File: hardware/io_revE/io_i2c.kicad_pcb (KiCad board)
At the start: 2 copper layers, 103.6 x 74.9 mm, 61 parts, among them J1 extra CS, J12 Conn_01x01, J13 Conn_01x01, J14 Conn_01x01, J15 Conn_01x01, J16 Target Interface, 2716 Pinout, J2 Jumper Block, J3 Jumper Block, J4 Target Interface, 2716 Pinout, J5 read region, J6 Conn_01x01, J7 Conn_01x01, J8 Conn_01x01, Q1 2N7000, U1 2716, U2 74LS74, U3 74LS125, U4 74LS138, U6 MCP23018-E_SP, U7 74LS138

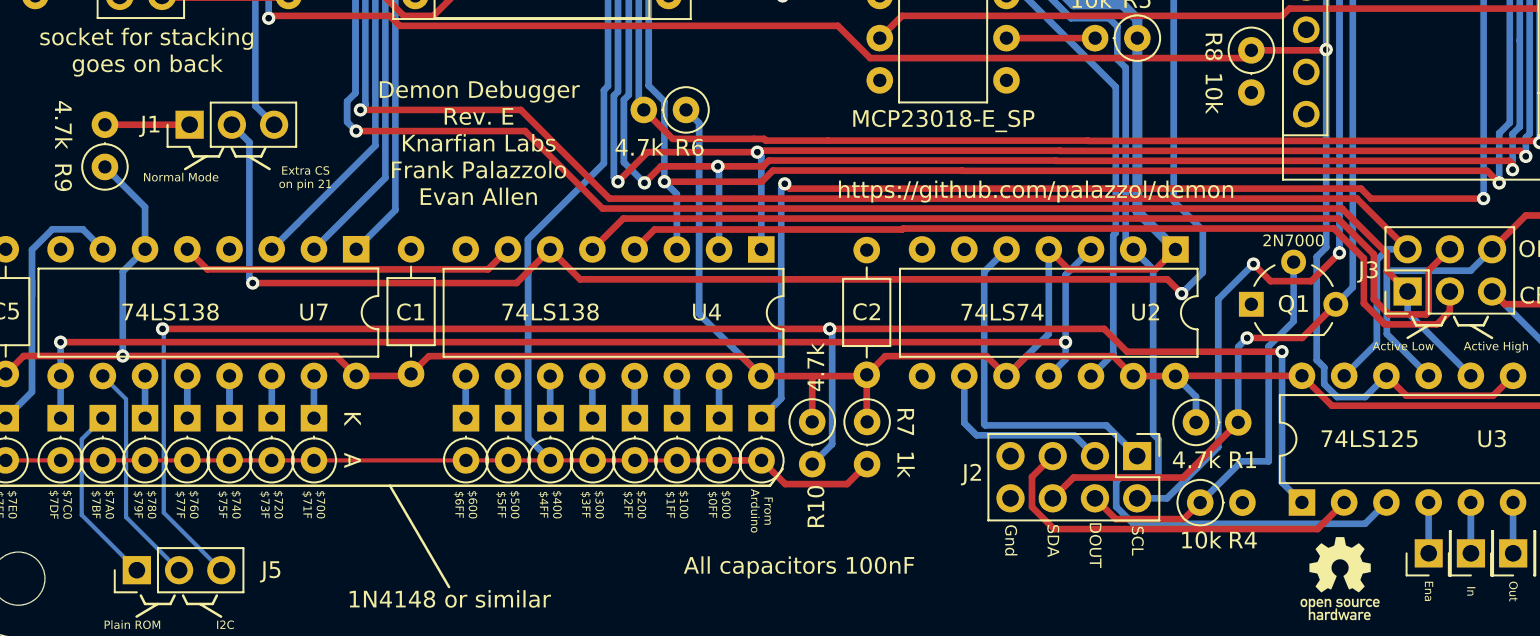
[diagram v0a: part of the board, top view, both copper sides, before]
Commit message: added pull up and silk changes
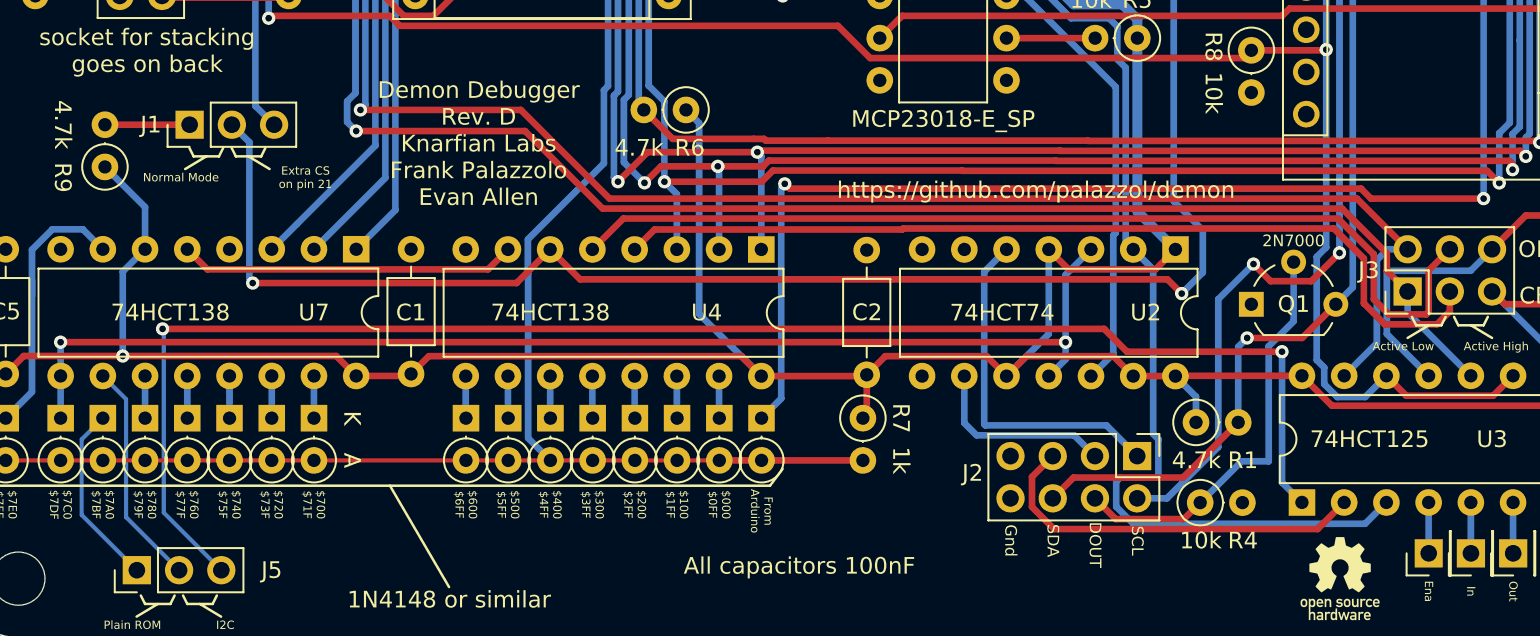
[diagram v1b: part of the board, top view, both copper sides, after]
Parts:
- removed R10: 4.7k, Resistor_THT:R_Axial_DIN0207_L6.3mm_D2.5mm_P2.54mm_Vertical
- U2: value 74LS74 -> 74HCT74
- U3: value 74LS125 -> 74HCT125
- U4, U7: value 74LS138 -> 74HCT138
- moved R7 0.34 mm to (138.9, 155.4)
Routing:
- net Net-(J5-Pad3): track 102.1 -> 93.5 mm, vias 3 -> 2
- net +5V: track 280.9 -> 278.1 mm
- net Net-(D10-Pad2): track 108.3 -> 107.0 mm
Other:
- board text added: "Demon Debugger Rev. D Knarfian Labs Frank Palazzolo Evan Allen"
- board text removed: "Demon Debugger Rev. E Knarfian Labs Frank Palazzolo Evan Allen"
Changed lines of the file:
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@@
       (effects (font (size 1 1) (thickness 0.15)))
     )
-    (fp_text value "74LS138" (at 3.81 11.176 180) (layer "F.SilkS")
+    (fp_text value "74HCT138" (at 3.81 11.176 180) (layer "F.SilkS")
       (effects (font (size 1 1) (thickness 0.15)))
     )
@@
   )
   (footprint "Resistor_THT:R_Axial_DIN0207_L6.3mm_D2.5mm_P2.54mm_Vertical" (layer "F.Cu")
-    (at 135.89 155.673 -90)
-    (descr "Resistor, Axial_DIN0207 series, Axial, Vertical, pin pitch=2.54mm, 0.25W = 1/4W, length*diameter=6.3*2.5mm^2, http://cdn-reichelt.de/documents/datenblatt/B400/1_4W%23YAG.pdf")
-    (tags "Resistor Axial_DIN0207 series Axial Vertical pin pitch 2.54mm 0.25W = 1/4W length 6.3mm diameter 2.5mm")
-    (property "Sheetfile" "io_i2c.kicad_sch")
-    (property "Sheetname" "")
-    (attr through_hole)
-    (fp_text reference "R10" (at 5.109 -0.254 90) (layer "F.SilkS")
-      (effects (font (size 1 1) (thickness 0.15)))
-    )
-    (fp_text value "4.7k" (at -3.273 -0.254 90) (layer "F.SilkS")
-      (effects (font (size 1 1) (thickness 0.15)))
-    )
-    (fp_text user "${REFERENCE}" (at 1.27 -2.37 90) (layer "F.Fab")
-      (effects (font (size 1 1) (thickness 0.15)))
-    )
-    (fp_line (start 1.37 0) (end 1.44 0) (layer "F.SilkS") (width 0.12))
-    (fp_circle (center 0 0) (end 1.37 0) (layer "F.SilkS") (width 0.12) (fill none))
-    (fp_line (start -1.5 1.5) (end 3.59 1.5) (layer "F.CrtYd") (width 0.05))
-    (fp_line (start 3.59 1.5) (end 3.59 -1.5) (layer "F.CrtYd") (width 0.05))
-    (fp_line (start -1.5 -1.5) (end -1.5 1.5) (layer "F.CrtYd") (width 0.05))
-    (fp_line (start 3.59 -1.5) (end -1.5 -1.5) (layer "F.CrtYd") (width 0.05))
-    (fp_line (start 0 0) (end 2.54 0) (layer "F.Fab") (width 0.1))
-    (fp_circle (center 0 0) (end 1.25 0) (layer "F.Fab") (width 0.1) (fill none))
-    (pad "1" thru_hole circle locked (at 0 0 270) (size 1.6 1.6) (drill 0.8) (layers *.Cu *.Mask)
-      (net 3 "+5V") (pintype "passive"))
-    (pad "2" thru_hole oval locked (at 2.54 0 270) (size 1.6 1.6) (drill 0.8) (layers *.Cu *.Mask)
-      (net 91 "Net-(J5-Pad3)") (pintype "passive"))
-    (model "${KICAD6_3DMODEL_DIR}/Resistor_THT.3dshapes/R_Axial_DIN0207_L6.3mm_D2.5mm_P2.54mm_Vertical.wrl"
-      (offset (xyz 0 0 0))
-      (scale (xyz 1 1 1))
-      (rotate (xyz 0 0 0))
-    )
-  )
-  (footprint "Resistor_THT:R_Axial_DIN0207_L6.3mm_D2.5mm_P2.54mm_Vertical" (layer "F.Cu")
     (at 182.851 143.256)
     (descr "Resistor, Axial_DIN0207 series, Axial, Vertical, pin pitch=2.54mm, 0.25W = 1/4W, length*diameter=6.3*2.5mm^2, http://cdn-reichelt.de/documents/datenblatt/B400/1_4W%23YAG.pdf")
@@
       (effects (font (size 1 1) (thickness 0.15)))
     )
-    (fp_text value "74LS74" (at 3.81 10.419 180) (layer "F.SilkS")
+    (fp_text value "74HCT74" (at 3.81 10.419 180) (layer "F.SilkS")
       (effects (font (size 1 1) (thickness 0.15)))
     )
@@
       (effects (font (size 1 1) (thickness 0.15)))
     )
-    (fp_text value "74LS138" (at 3.8 12.685 180) (layer "F.SilkS")
+    (fp_text value "74HCT138" (at 3.8 12.685 180) (layer "F.SilkS")
       (effects (font (size 1 1) (thickness 0.15)))
     )
@@
       (effects (font (size 1 1) (thickness 0.15)))
     )
-    (fp_text value "74LS125" (at 3.8 4.069 180) (layer "F.SilkS")
+    (fp_text value "74HCT125" (at 3.8 4.069 180) (layer "F.SilkS")
       (effects (font (size 1 1) (thickness 0.15)))
     )
@@
   )
   (footprint "Resistor_THT:R_Axial_DIN0207_L6.3mm_D2.5mm_P2.54mm_Vertical" (layer "F.Cu")
-    (at 139.192 155.673 -90)
+    (at 138.938 155.448 -90)
     (descr "Resistor, Axial_DIN0207 series, Axial, Vertical, pin pitch=2.54mm, 0.25W = 1/4W, length*diameter=6.3*2.5mm^2, http://cdn-reichelt.de/documents/datenblatt/B400/1_4W%23YAG.pdf")
     (tags "Resistor Axial_DIN0207 series Axial Vertical pin pitch 2.54mm 0.25W = 1/4W length 6.3mm diameter 2.5mm")
@@
     (effects (font (size 0.5 0.5) (thickness 0.05)))
   )
-  (gr_text "Demon Debugger\nRev. E\nKnarfian Labs\nFrank Palazzolo\nEvan Allen" (at 115.824 138.938) (layer "F.SilkS")
+  (gr_text "Demon Debugger\nRev. D\nKnarfian Labs\nFrank Palazzolo\nEvan Allen" (at 115.824 138.938) (layer "F.SilkS")
     (effects (font (size 1 1) (thickness 0.15)))
   )
@@
   (segment (start 157.759 152.898) (end 157.739 152.918) (width 0.4) (layer "F.Cu") (net 3))
   (segment (start 111.64 152.908) (end 111.76 152.788) (width 0.4) (layer "F.Cu") (net 3))
-  (segment (start 132.827 152.918) (end 135.88 152.918) (width 0.4) (layer "F.Cu") (net 3))
   (segment (start 167.148031 154.697031) (end 165.349 152.898) (width 0.4) (layer "F.Cu") (net 3))
+  (segment (start 132.827 152.918) (end 139.089 152.918) (width 0.4) (layer "F.Cu") (net 3))
   (segment (start 108.458 152.908) (end 111.64 152.908) (width 0.4) (layer "F.Cu") (net 3))
   (segment (start 147.579 152.918) (end 148.778511 151.718489) (width 0.4) (layer "F.Cu") (net 3))
@@
   (segment (start 94.417511 151.708489) (end 88.455511 151.708489) (width 0.4) (layer "F.Cu") (net 3))
   (segment (start 146.379489 151.718489) (end 147.579 152.918) (width 0.4) (layer "F.Cu") (net 3))
-  (segment (start 135.89 155.673) (end 135.89 152.928) (width 0.4) (layer "F.Cu") (net 3))
   (segment (start 138.684 98.806) (end 159.512 98.806) (width 1) (layer "F.Cu") (net 3))
   (segment (start 151.318511 146.497511) (end 150.119 145.298) (width 0.4) (layer "F.Cu") (net 3))
@@
   (segment (start 153.999489 151.718489) (end 155.199 152.918) (width 0.4) (layer "F.Cu") (net 3))
   (segment (start 165.349 152.898) (end 157.759 152.898) (width 0.4) (layer "F.Cu") (net 3))
-  (segment (start 135.89 152.928) (end 135.88 152.918) (width 0.4) (layer "F.Cu") (net 3))
   (segment (start 156.539489 146.497511) (end 151.318511 146.497511) (width 0.4) (layer "F.Cu") (net 3))
   (segment (start 139.954 127.508) (end 141.224 126.238) (width 0.4) (layer "F.Cu") (net 3))
@@
   (segment (start 151.303511 151.718489) (end 153.999489 151.718489) (width 0.4) (layer "F.Cu") (net 3))
   (segment (start 105.664 98.806) (end 127.254 98.806) (width 1) (layer "F.Cu") (net 3))
-  (segment (start 135.88 152.918) (end 139.089 152.918) (width 0.4) (layer "F.Cu") (net 3))
   (segment (start 139.169 152.838) (end 140.288511 151.718489) (width 0.4) (layer "F.Cu") (net 3))
   (segment (start 183.896 153.028) (end 182.226969 154.697031) (width 0.4) (layer "F.Cu") (net 3))
@@
   (segment (start 116.387489 146.497511) (end 99.507511 146.497511) (width 0.4) (layer "F.Cu") (net 79))
   (segment (start 87.376 157.988) (end 90.678 157.988) (width 0.25) (layer "F.Cu") (net 80))
-  (segment (start 137.992489 159.412511) (end 139.192 158.213) (width 0.4) (layer "F.Cu") (net 80))
+  (segment (start 132.842 157.988) (end 138.938 157.988) (width 0.4) (layer "F.Cu") (net 80))
   (segment (start 93.218 157.988) (end 95.758 157.988) (width 0.25) (layer "F.Cu") (net 80))
-  (segment (start 134.266511 159.412511) (end 137.992489 159.412511) (width 0.4) (layer "F.Cu") (net 80))
   (segment (start 90.678 157.988) (end 93.218 157.988) (width 0.25) (layer "F.Cu") (net 80))
   (segment (start 95.758 157.988) (end 132.842 157.988) (width 0.25) (layer "F.Cu") (net 80))
   (segment (start 130.302 157.988) (end 132.842 157.988) (width 0.4) (layer "F.Cu") (net 80))
-  (segment (start 132.842 157.988) (end 134.266511 159.412511) (width 0.4) (layer "F.Cu") (net 80))
   (segment (start 127.254 112.268) (end 122.936 112.268) (width 0.4) (layer "F.Cu") (net 80))
   (via (at 122.936 112.268) (size 0.8) (drill 0.4) (layers "F.Cu" "B.Cu") (net 80))
@@
   (segment (start 175.509 163.571) (end 175.514 163.576) (width 0.4) (layer "B.Cu") (net 90))
   (segment (start 164.149489 151.449489) (end 154.826511 151.449489) (width 0.4) (layer "F.Cu") (net 91))
-  (segment (start 136.943511 150.076489) (end 96.811511 150.076489) (width 0.4) (layer "F.Cu") (net 91))
-  (segment (start 153.453511 150.076489) (end 136.943511 150.076489) (width 0.4) (layer "F.Cu") (net 91))
+  (segment (start 153.453511 150.076489) (end 96.811511 150.076489) (width 0.4) (layer "F.Cu") (net 91))
   (segment (start 154.826511 151.449489) (end 153.453511 150.076489) (width 0.4) (layer "F.Cu") (net 91))
-  (via (at 136.943511 150.076489) (size 0.8) (drill 0.4) (layers "F.Cu" "B.Cu") (net 91))
   (via (at 164.149489 151.449489) (size 0.8) (drill 0.4) (layers "F.Cu" "B.Cu") (net 91))
   (via (at 96.811511 150.076489) (size 0.8) (drill 0.4) (layers "F.Cu" "B.Cu") (net 91))
@@
   (segment (start 96.882511 150.147489) (end 96.882511 161.129511) (width 0.25) (layer "B.Cu") (net 91))
   (segment (start 164.149489 159.318489) (end 164.149489 151.449489) (width 0.4) (layer "B.Cu") (net 91))
-  (segment (start 137.089511 150.297511) (end 136.906 150.114) (width 0.4) (layer "B.Cu") (net 91))
-  (segment (start 135.89 158.213) (end 137.089511 157.013489) (width 0.4) (layer "B.Cu") (net 91))
   (segment (start 96.882511 161.129511) (end 100.345 164.592) (width 0.25) (layer "B.Cu") (net 91))
-  (segment (start 137.089511 157.013489) (end 137.089511 150.297511) (width 0.4) (layer "B.Cu") (net 91))
   (zone (net 1) (net_name "GND") (layers F&B.Cu) (hatch edge 0.508)
     (connect_pads (clearance 0.508))
